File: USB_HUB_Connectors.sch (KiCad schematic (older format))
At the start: 81 parts, among them J11 WE_632723300011, J13 WE_632723300011, U15 USB57442G, Y2 ABM8G-25.000MHZ-B4Y-T

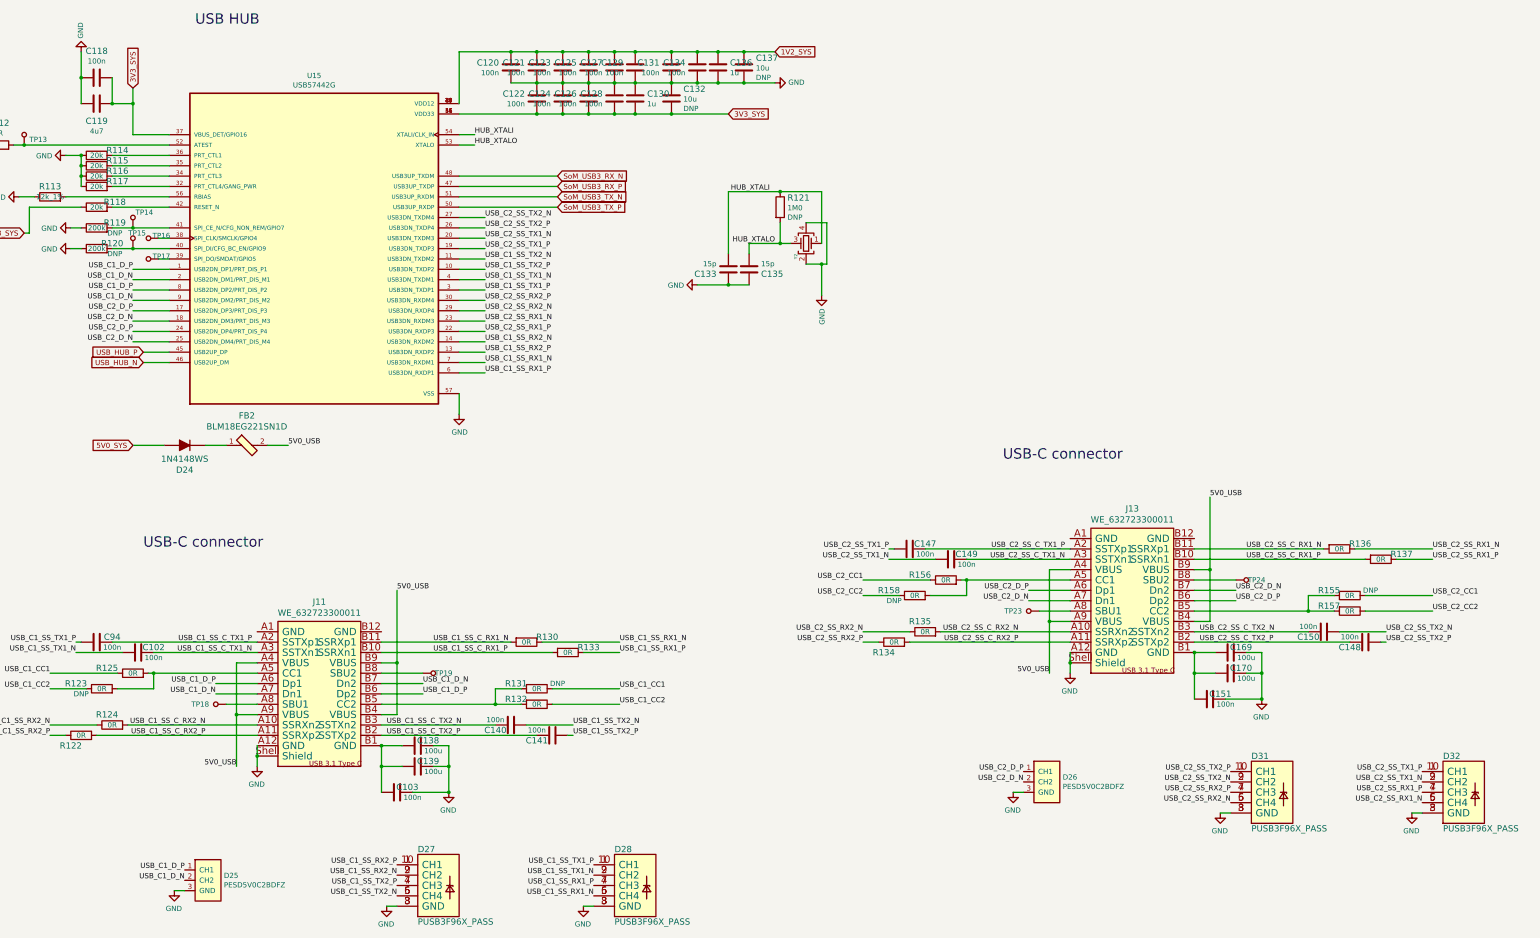
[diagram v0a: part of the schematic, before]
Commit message: All components placed on board
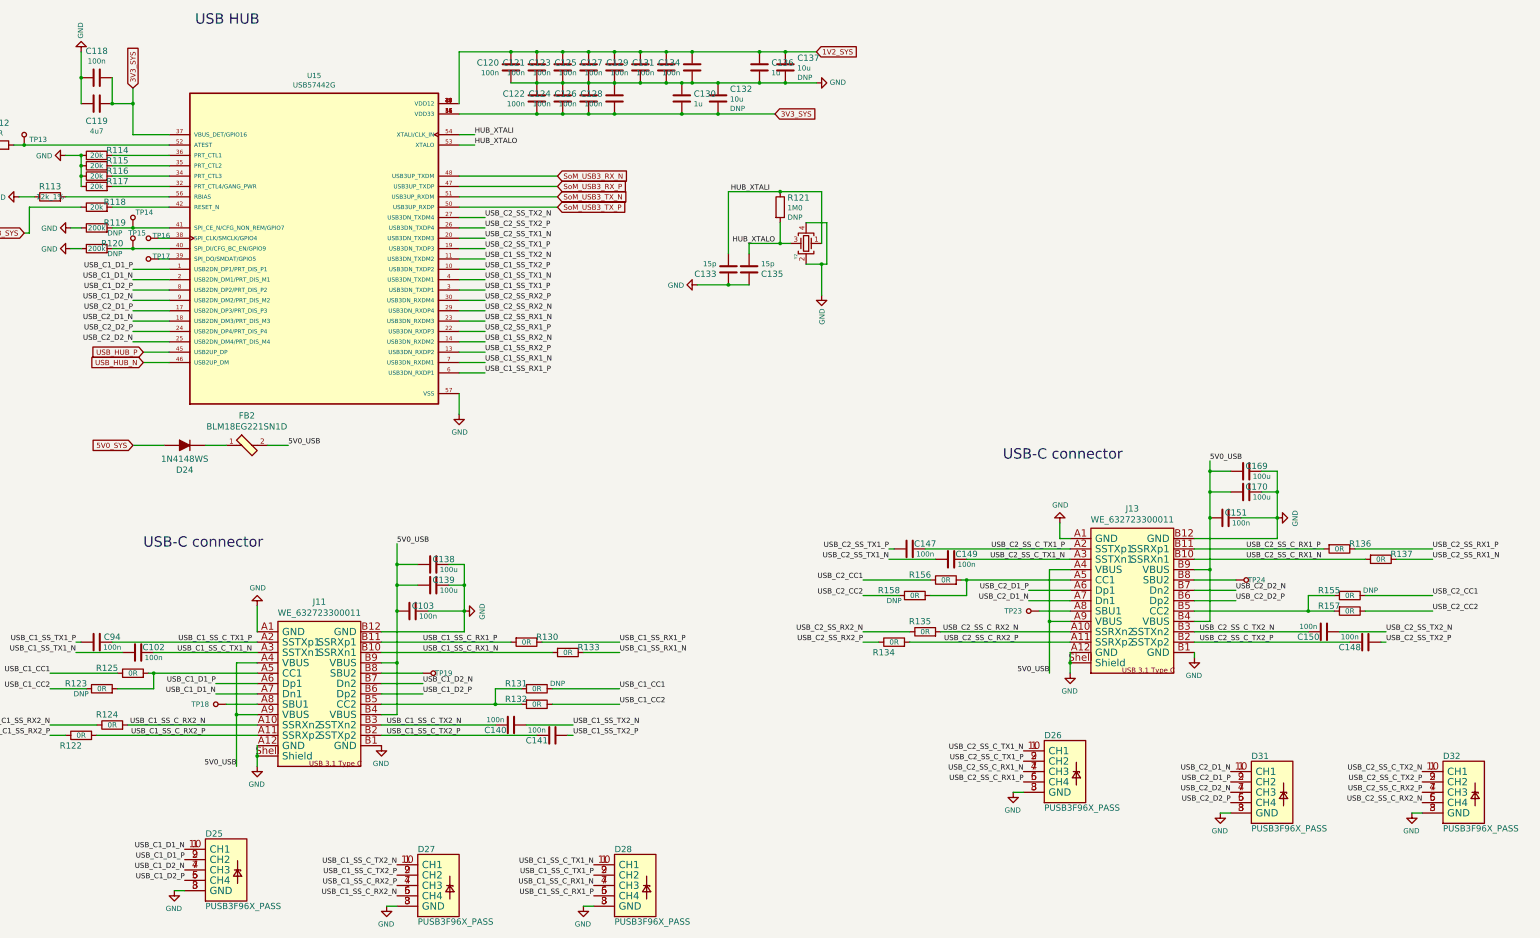
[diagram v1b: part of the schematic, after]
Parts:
- removed D25, D26: PESD5V0C2BDFZ, sc606-baseboard-footprints:DFN0603-3, symbol sc606-baseboard:PESD5V0C2BDFZ
- added D25, D26: PUSB3F96X_PASS, sc606-baseboard-footprints:PUSB3F96X, symbol sc606-baseboard:PUSB3F96X_PASS
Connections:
- net 5V0_USB: now also C103.2, C138.2, C139.2, C151.2, C169.2, C170.2
- net GND: now also J11.A1 (GND), J11.B1 (GND), J11.B12 (GND), J13.A1 (GND), J13.B1 (GND), J13.B12 (GND), D25.3 (GND), D25.8 (GND), D26.3 (GND), D26.8 (GND)
- net USB_C1_SS_C_RX1_N: now also D28.4 (CH3), D28.7 (CH3), J11.B10 (SSRXn1), R133.2; no longer J11.B11 (SSRXp1), R130.2
- net USB_C1_SS_C_RX1_P: now also D28.5 (CH4), D28.6 (CH4), J11.B11 (SSRXp1), R130.2; no longer J11.B10 (SSRXn1), R133.2
- net USB_C1_SS_C_RX2_N: now also D27.5 (CH4), D27.6 (CH4)
- net USB_C1_SS_C_RX2_P: now also D27.4 (CH3), D27.7 (CH3)
- net USB_C1_SS_C_TX1_N: now also D28.1 (CH1), D28.10 (CH1)
- net USB_C1_SS_C_TX1_P: now also D28.2 (CH2), D28.9 (CH2)
- net USB_C1_SS_C_TX2_N: now also D27.1 (CH1), D27.10 (CH1)
- net USB_C1_SS_C_TX2_P: now also D27.2 (CH2), D27.9 (CH2)
- net USB_C1_SS_RX1_N: now also R133.1; no longer D28.5 (CH4), D28.6 (CH4), R130.1
- net USB_C1_SS_RX1_P: now also R130.1; no longer D28.4 (CH3), D28.7 (CH3), R133.1
- net USB_C1_SS_RX2_N: no longer D27.2 (CH2), D27.9 (CH2)
- net USB_C1_SS_RX2_P: no longer D27.1 (CH1), D27.10 (CH1)
- net USB_C1_SS_TX1_N: no longer D28.2 (CH2), D28.9 (CH2)
- net USB_C1_SS_TX1_P: no longer D28.1 (CH1), D28.10 (CH1)
- net USB_C1_SS_TX2_N: no longer D27.5 (CH4), D27.6 (CH4)
- net USB_C1_SS_TX2_P: no longer D27.4 (CH3), D27.7 (CH3)
- net USB_C2_SS_C_RX1_N: now also J13.B10 (SSRXn1), R137.2, D26.4 (CH3), D26.7 (CH3); no longer J13.B11 (SSRXp1), R136.2
- net USB_C2_SS_C_RX1_P: now also J13.B11 (SSRXp1), R136.2, D26.5 (CH4), D26.6 (CH4); no longer J13.B10 (SSRXn1), R137.2
- net USB_C2_SS_C_RX2_N: now also D32.5 (CH4), D32.6 (CH4)
- net USB_C2_SS_C_RX2_P: now also D32.4 (CH3), D32.7 (CH3)
- net USB_C2_SS_C_TX1_N: now also D26.1 (CH1), D26.10 (CH1)
- net USB_C2_SS_C_TX1_P: now also D26.2 (CH2), D26.9 (CH2)
- net USB_C2_SS_C_TX2_N: now also D32.1 (CH1), D32.10 (CH1)
- net USB_C2_SS_C_TX2_P: now also D32.2 (CH2), D32.9 (CH2)
- net USB_C2_SS_RX1_N: now also R137.1; no longer D32.5 (CH4), D32.6 (CH4), R136.1
- net USB_C2_SS_RX1_P: now also R136.1; no longer D32.4 (CH3), D32.7 (CH3), R137.1
- net USB_C2_SS_RX2_N: no longer D31.5 (CH4), D31.6 (CH4)
- net USB_C2_SS_RX2_P: no longer D31.4 (CH3), D31.7 (CH3)
- net USB_C2_SS_TX1_N: no longer D32.2 (CH2), D32.9 (CH2)
- net USB_C2_SS_TX1_P: no longer D32.1 (CH1), D32.10 (CH1)
- net USB_C2_SS_TX2_N: no longer D31.2 (CH2), D31.9 (CH2)
- net USB_C2_SS_TX2_P: no longer D31.1 (CH1), D31.10 (CH1)
- net USB_C1_D_N renamed USB_C1_D1_N
- net USB_C1_D1_N: now also D25.1 (CH1), D25.10 (CH1); no longer J11.B7 (Dn2), U15.9 (USB2DN_DM2/PRT_DIS_M2)
- net USB_C1_D_P renamed USB_C1_D1_P
- net USB_C1_D1_P: now also D25.2 (CH2), D25.9 (CH2); no longer J11.B6 (Dp2), U15.8 (USB2DN_DP2/PRT_DIS_P2)
- net USB_C2_D_N renamed USB_C2_D1_N
- net USB_C2_D1_N: now also D31.1 (CH1), D31.10 (CH1); no longer J13.B7 (Dn2), U15.25 (USB2DN_DM4/PRT_DIS_M4)
- net USB_C2_D_P renamed USB_C2_D1_P
- net USB_C2_D1_P: now also D31.2 (CH2), D31.9 (CH2); no longer J13.B6 (Dp2), U15.24 (USB2DN_DP4/PRT_DIS_P4)
- new net USB_C1_D2_N: D25.4 (CH3), D25.7 (CH3), J11.B7 (Dn2), U15.9 (USB2DN_DM2/PRT_DIS_M2)
- new net USB_C1_D2_P: D25.5 (CH4), D25.6 (CH4), J11.B6 (Dp2), U15.8 (USB2DN_DP2/PRT_DIS_P2)
- new net USB_C2_D2_N: D31.4 (CH3), D31.7 (CH3), J13.B7 (Dn2), U15.25 (USB2DN_DM4/PRT_DIS_M4)
- new net USB_C2_D2_P: D31.5 (CH4), D31.6 (CH4), J13.B6 (Dp2), U15.24 (USB2DN_DP4/PRT_DIS_P4)
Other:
- moved on the sheet: C103, C129, C130, C131, C132, C134, C136, C137, C138, C139, C151, C169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

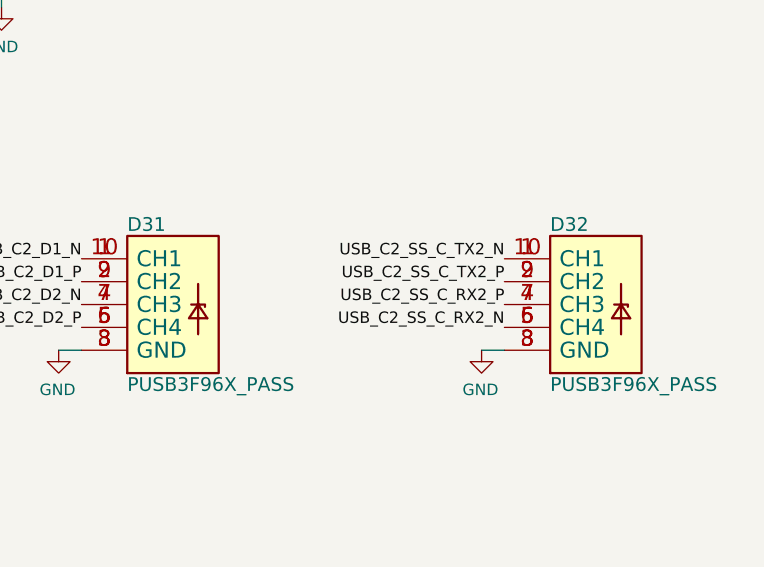
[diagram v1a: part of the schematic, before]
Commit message: USB Debug changed to micro USB. Started modifications on shortening board by 1cm
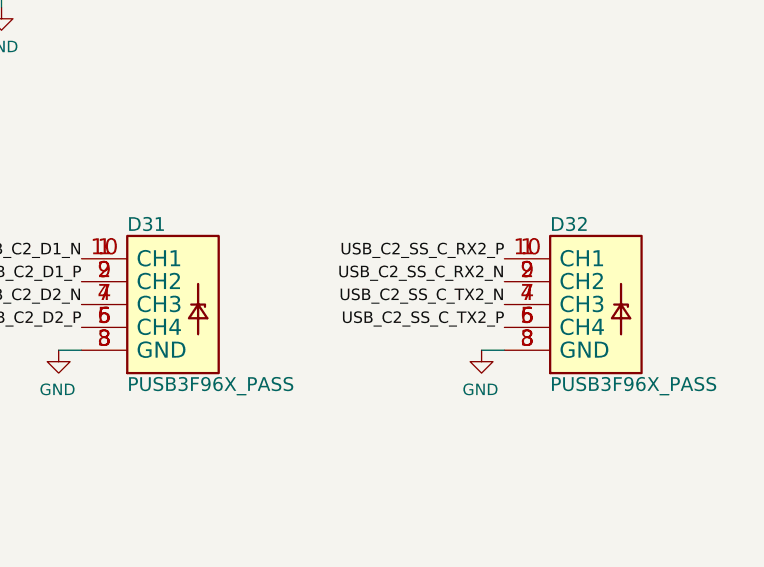
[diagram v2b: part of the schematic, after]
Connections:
- net USB_C2_SS_C_RX2_N: now also D32.2 (CH2), D32.9 (CH2); no longer D32.5 (CH4), D32.6 (CH4)
- net USB_C2_SS_C_RX2_P: now also D32.1 (CH1), D32.10 (CH1); no longer D32.4 (CH3), D32.7 (CH3)
- net USB_C2_SS_C_TX2_N: now also D32.4 (CH3), D32.7 (CH3); no longer D32.1 (CH1), D32.10 (CH1)
- net USB_C2_SS_C_TX2_P: now also D32.5 (CH4), D32.6 (CH4); no longer D32.2 (CH2), D32.9 (CH2)
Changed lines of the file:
@@
 	-1   0    0    -1
 $EndComp
+Text Label 14900 8250 2    50   ~ 0
+USB_C2_SS_C_RX2_N
+Text Label 14900 8150 2    50   ~ 0
+USB_C2_SS_C_RX2_P
+Text Label 14900 8350 2    50   ~ 0
+USB_C2_SS_C_TX2_N
 Text Label 14900 8450 2    50   ~ 0
-USB_C2_SS_C_RX2_N
-Text Label 14900 8350 2    50   ~ 0
-USB_C2_SS_C_RX2_P
-Text Label 14900 8150 2    50   ~ 0
-USB_C2_SS_C_TX2_N
-Text Label 14900 8250 2    50   ~ 0
 USB_C2_SS_C_TX2_P
 $Comp

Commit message: Finished placement after shortening board by 1cm
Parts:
- removed R123, R125, R131, R132, R155, R156, R157, R158: R_0R_0402, sc606-baseboard-footprints:0402-res, symbol sc606-baseboard:R_0R_0402
- added R? (x8): R_56k_0402, antmicro-footprints:0402-res, symbol antmicroResistors0402:R_56k_0402
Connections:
- wire segments 235 -> 219

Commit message: Changed USB flash and debug to USB-C. Prepared place for USB PD. Minor modifications of components position
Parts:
- removed J11, J13: WE_632723300011, sc606-baseboard-footprints:WE_632723300011, symbol sc606-baseboard:WE_632723300011
- added J10, J11: E8124-015-01, sc606-baseboard-footprints:USB-C_Female_E8124-015-01, symbol sc606-baseboard:E8124-015-01
- R123, R125, R131, R132, R138, R139, R140, R141: renamed from R?; footprint antmicro-footprints:0402-res -> sc606-baseboard-footprints:0402-res; symbol antmicroResistors0402:R_56k_0402 -> sc606-baseboard:R_56k_0402
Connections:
- wire segments 219 -> 217
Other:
- moved on the sheet: C102, C147, C149, C94, R122, R124, R134, R135, TP18, TP23

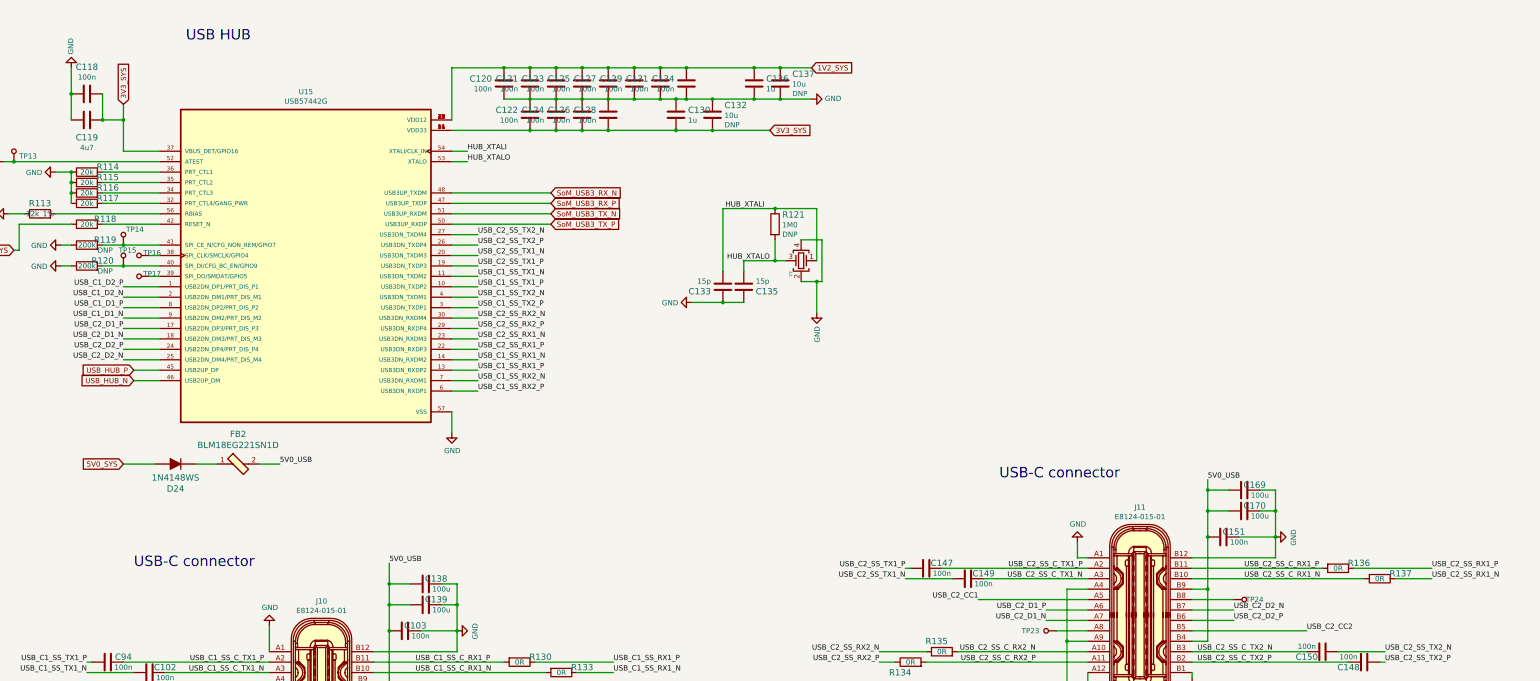
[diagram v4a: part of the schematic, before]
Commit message: Changed ESD diode and transistor near USB-PD
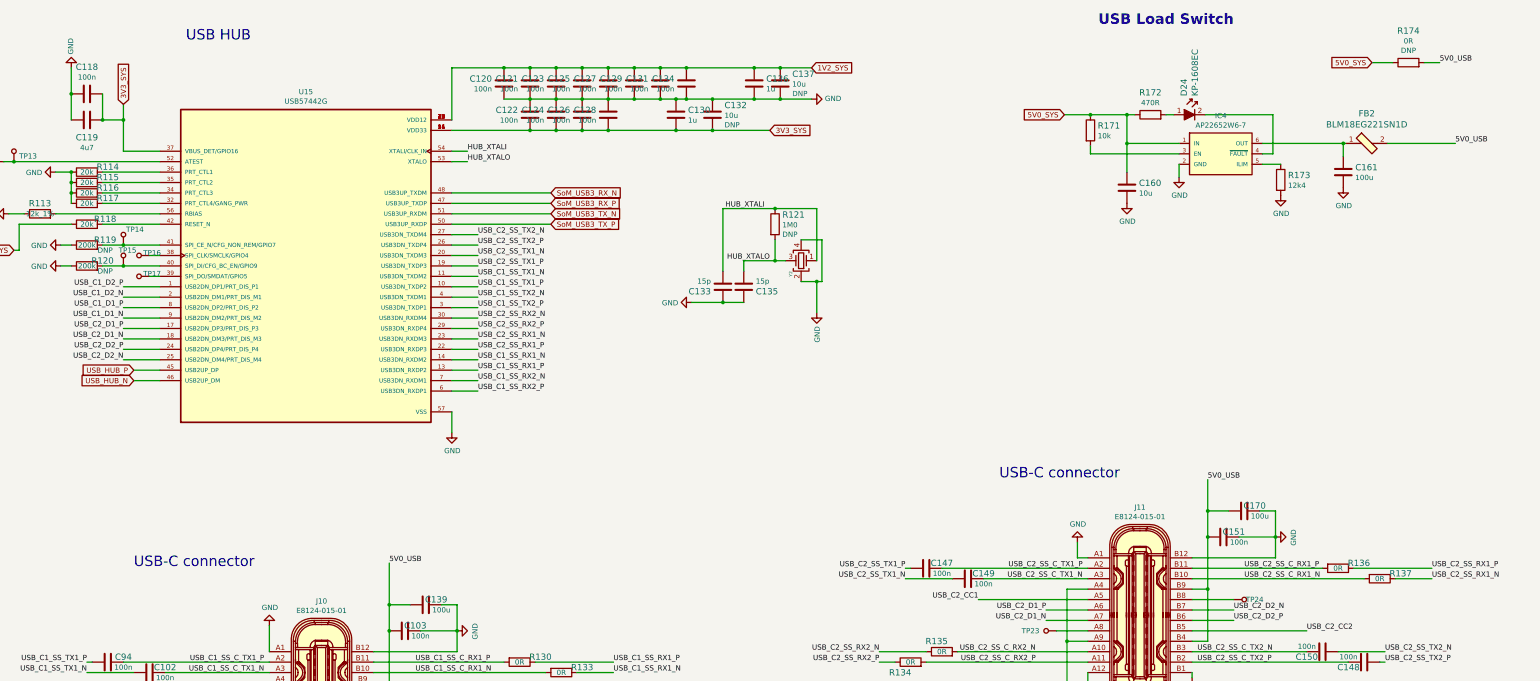
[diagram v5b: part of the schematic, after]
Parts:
- removed C138, C169: C_100u_0805, sc606-baseboard-footprints:0805-cap, symbol sc606-baseboard:C_100u_0805
- removed D24: 1N4148WS, sc606-baseboard-footprints:SOD-323F, symbol sc606-baseboard:1N4148WS
- removed FB2: BLM18EG221SN1D, sc606-baseboard-footprints:0603, symbol sc606-baseboard:BLM18EG221SN1D
- added C160: C_10u_0402, antmicro-footprints:0402-cap, symbol antmicroCapacitors0402:C_10u_0402
- added C161: C_100u_0805, antmicro-footprints:0805-cap, symbol antmicroCapacitorsmisc:C_100u_0805
- added D24: KP-1608EC, sc606-baseboard-footprints:LED_0603, symbol sc606-baseboard:KP-1608EC
- added FB2: BLM18EG221SN1D, antmicro-footprints:0603, symbol antmicroFerriteBeadsandChips:BLM18EG221SN1D
- added IC4: AP22652W6-7, antmicro-footprints:SOT-23-6, symbol antmicroPMICPowerDistributionSwitchesLoadDrivers:AP22652W6-7
- added R171: R_10k_0402, antmicro-footprints:0402-res, symbol antmicroResistors0402:R_10k_0402
- added R172: R_470R_0402, antmicro-footprints:0402-res, symbol antmicroResistors0402:R_470R_0402
- added R173: R_12k4_0402, antmicro-footprints:0402-res, symbol antmicroResistors0402:R_12k4_0402
- added R174: R_0R_0402, antmicro-footprints:0402-res, symbol antmicroResistors0402:R_0R_0402
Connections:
- net 5V0_SYS: now also C160.1, IC4.1 (IN), R171.1, R172.1, R174.1
- net 5V0_USB: now also FB2.2, R174.2
- net GND: now also C160.2, C161.2, IC4.2 (GND), R173.2
- new net: IC4.3 (EN), R171.2
- new net: D24.2, IC4.4 (~FAULT~)
- new net: IC4.5 (ILIM), R173.1
- new net: C161.1, FB2.1, IC4.6 (OUT)
- new net: D24.1, R172.2
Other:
- note added: "USB Load Switch"
